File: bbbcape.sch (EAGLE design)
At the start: 25 parts

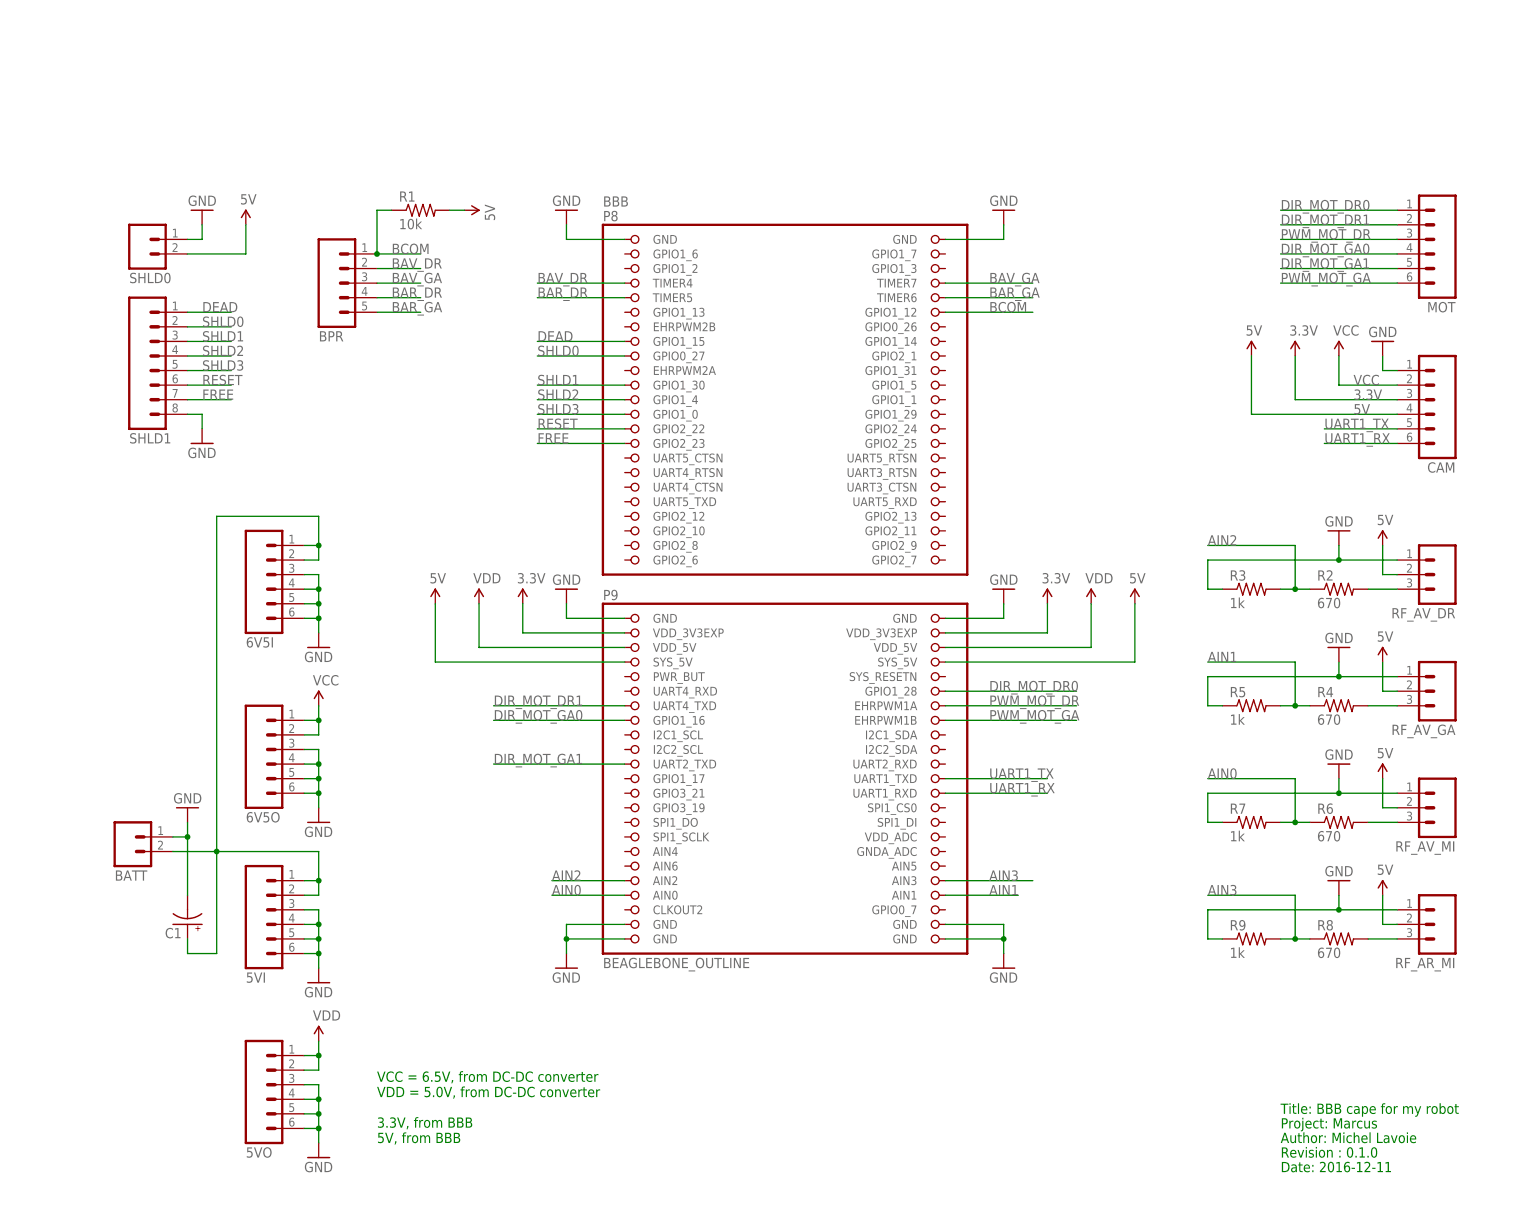
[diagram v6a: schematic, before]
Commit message: Added and connected firing circuit.
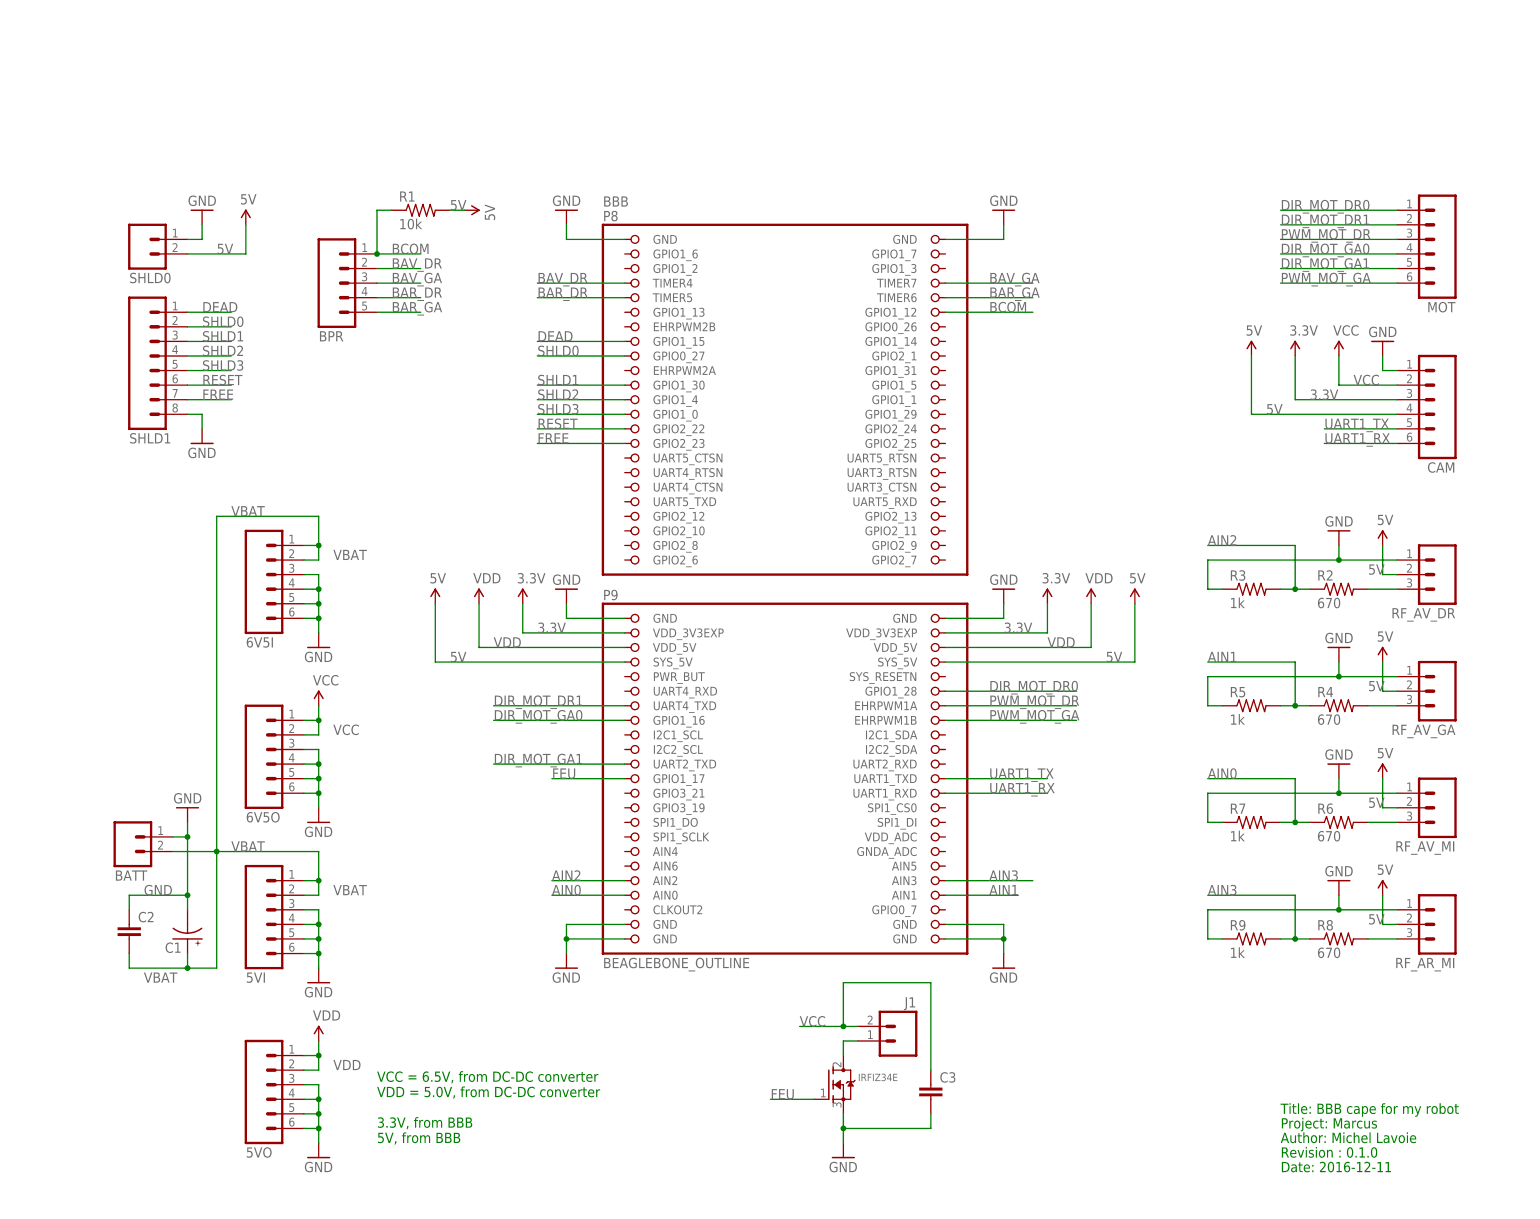
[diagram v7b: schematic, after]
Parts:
- added C2, C3: (no value), SparkFun-Capacitors:0.1UF-50V-20%(PTH)KIT-EZ
- added IRFIZ34E: (no value), adafruit:MOSFET-NGDS_TO220V
- added J1: (no value), SparkFun-Connectors:M02PTH
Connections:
- removed net 6V5: 6V5O.1, 6V5O.2
- removed net N$1: 5VI.1, 5VI.2, 6V5I.1, 6V5I.2, BATT.2, C1.+
- new net FEU: BBB.GPIO1_17, IRFIZ34E.G
- new net N$3: IRFIZ34E.D, J1.1
- new net VBAT: 5VI.1, 5VI.2, 6V5I.1, 6V5I.2, BATT.2, C1.+, C2.2
- net GND: now also C2.1, C3.2, IRFIZ34E.S
- net VCC: now also 6V5O.1, 6V5O.2, C3.1, J1.2
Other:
- moved on the sheet: C1

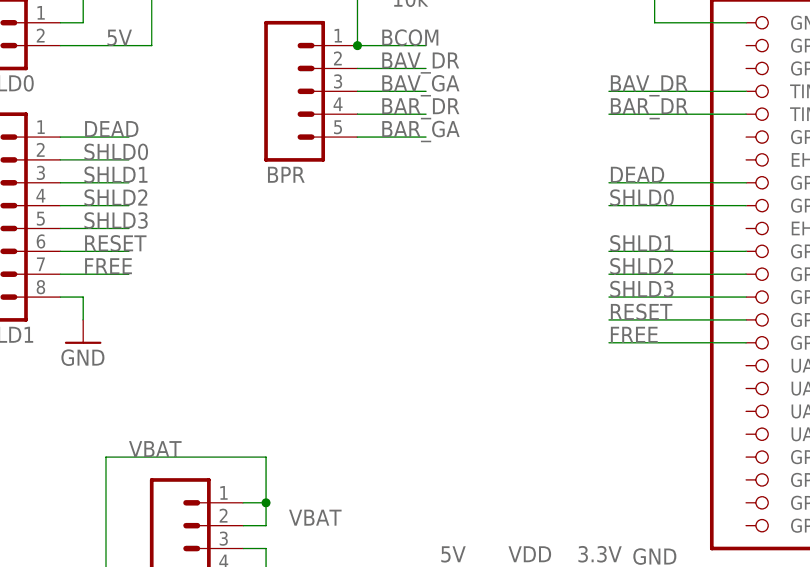
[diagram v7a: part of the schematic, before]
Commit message: Added reset button (on BAR_GA, P8_10).
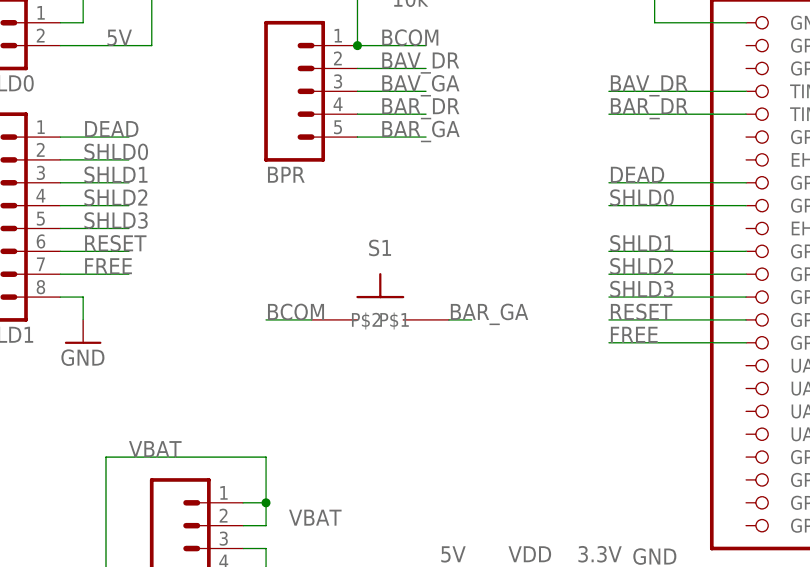
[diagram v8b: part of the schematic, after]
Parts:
- added S1: TACTILE-SPST-6MM-SLIM, michel:TACTILE-SPST-6MM-SLIM
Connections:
- net BAR_GA: now also S1.P$2
- net BCOM: now also S1.P$1
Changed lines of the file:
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@@
 <setting verticaltext="up"/>
 </settings>
-<grid distance="0.1" unitdist="inch" unit="inch" style="dots" multiple="1" display="yes" altdistance="0.01" altunitdist="inch" altunit="inch"/>
+<grid distance="0.1" unitdist="inch" unit="inch" style="lines" multiple="1" display="no" altdistance="0.01" altunitdist="inch" altunit="inch"/>
 <layers>
 <layer number="1" name="Top" color="4" fill="1" visible="no" active="no"/>
@@
 <part name="GND19" library="SparkFun-Aesthetics" deviceset="GND" device=""/>
 <part name="C3" library="SparkFun-Capacitors" deviceset="0.1UF-50V-20%(PTH)" device="KIT-EZ"/>
+<part name="S1" library="michel" deviceset="TACTILE-SPST-6MM-SLIM" device=""/>
 </parts>
 <sheets>
@@
 <instance part="GND19" gate="1" x="134.62" y="10.16"/>
 <instance part="C3" gate="G$1" x="149.86" y="20.32"/>
+<instance part="S1" gate="G$1" x="55.88" y="137.16" smashed="yes">
+<attribute name="NAME" x="55.88" y="144.272" size="1.778" layer="95" align="bottom-center"/>
+</instance>
 </instances>
 <busses>
@@
 <label x="160.02" y="157.48" size="1.778" layer="95"/>
 </segment>
+<segment>
+<pinref part="S1" gate="G$1" pin="P$1"/>
+<wire x1="43.18" y1="137.16" x2="48.26" y2="137.16" width="0.1524" layer="91"/>
+<label x="43.18" y="137.16" size="1.778" layer="95"/>
+</segment>
 </net>
 <net name="BAV_DR" class="0">
@@
 <label x="160.02" y="160.02" size="1.778" layer="95"/>
 </segment>
-</net>
+<segment>
+<pinref part="S1" gate="G$1" pin="P$2"/>
+<wire x1="66.04" y1="137.16" x2="63.5" y2="137.16" width="0.1524" layer="91"/>
+<label x="63.5" y="137.16" size="1.778" layer="95"/>
+</segment>
+</net>
